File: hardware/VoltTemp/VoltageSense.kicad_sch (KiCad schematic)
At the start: 31 parts, among them J4 bms i2c test, SW1 BMS_BOOT, U1 EL3H7, U2 BQ7692003PW, U3 EL3H7, U4 ISO1641BDR

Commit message: schematic mostly done
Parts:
- removed C1: 4.7pF, Capacitor_SMD:C_0805_2012Metric, symbol Device:C_Small
- removed C3, C5: 1μF, Capacitor_SMD:C_0805_2012Metric, symbol Device:C_Small
- removed C4: 4.7μF, Capacitor_SMD:C_0805_2012Metric, symbol Device:C_Small
- removed R1, R6: 10kΩ, Resistor_SMD:R_0805_2012Metric, symbol Device:R
- removed R3, R4: 100Ω, Resistor_SMD:R_0805_2012Metric, symbol Device:R
- removed R7: 1kΩ, Resistor_SMD:R_0805_2012Metric, symbol Device:R
- removed U1, U3: EL3H7, Package_SO:SSOP-4_4.4x2.6mm_P1.27mm, symbol Isolator:SFH617A-1
- removed U2: BQ7692003PW, footprints:PW0020A_N, symbol BQ76920:BQ7692003PW
- removed U4: ISO1641BDR, footprints:SOIC8_D_TEX, symbol ISO1541QDQ1:ISO1641BDR
- added C18: 4.7uF, Capacitor_SMD:C_0805_2012Metric_Pad1.18x1.45mm_HandSolder, symbol Device:C
- added C24, C42: 0.1uF, Capacitor_SMD:C_0603_1608Metric_Pad1.08x0.95mm_HandSolder, symbol Device:C
- added C4: 4.7pF, Capacitor_SMD:C_0603_1608Metric_Pad1.08x0.95mm_HandSolder, symbol Device:C
- added C40, C41: 1uF, Capacitor_SMD:C_0603_1608Metric_Pad1.08x0.95mm_HandSolder, symbol Device:C
- added IC1: ISO1641BDR, VoltTemp:ISO1641BDR, symbol voltTemp:ISO1641BDR
- added R11, R13: 10kΩ, Resistor_SMD:R_0603_1608Metric_Pad0.98x0.95mm_HandSolder, symbol Device:R
- added R12: 1kΩ, Resistor_SMD:R_0603_1608Metric_Pad0.98x0.95mm_HandSolder, symbol Device:R
- added R59, R60: 100Ω, Resistor_SMD:R_0603_1608Metric_Pad0.98x0.95mm_HandSolder, symbol Device:R
- added U1, U3: EL3H7, UTSVT_ICs:EL3H7, symbol utsvt_ics:EL3H7
- added U2: BQ7692003PW, VoltTemp:BQ7692003PW, symbol voltTemp:BQ7692003PW
- R10, R9: footprint Resistor_SMD:R_0805_2012Metric -> Resistor_SMD:R_0603_1608Metric_Pad0.98x0.95mm_HandSolder; P/N CRCW080510K0FKEAC -> CRCW060310K0FKEI
- R2: value 500kΩ -> 510kΩ; footprint Resistor_SMD:R_0805_2012Metric -> Resistor_SMD:R_0603_1608Metric_Pad0.98x0.95mm_HandSolder; P/N 708-RNCF0805BTE500K -> CPF0603B510KE1
- R25, R26, R27, R28: footprint Resistor_SMD:R_0805_2012Metric -> Resistor_SMD:R_0603_1608Metric_Pad0.98x0.95mm_HandSolder; P/N SMD_0805 -> (none)
- R8: footprint Resistor_SMD:R_0805_2012Metric -> Resistor_SMD:R_0603_1608Metric_Pad0.98x0.95mm_HandSolder; P/N CRCW08051K00FKEAC -> CRCW06031K00FKEI
- SW1: value BMS_BOOT -> BOOT; footprint Button_Switch_SMD:SW_SPST_B3SL-1002P -> VoltTemp:SW_TL3365AF180QG; P/N 653-B3SL-1002P -> TL3365AF180QG
- TP1, TP2, TP3, TP4, TP5: footprint (none) -> TestPoint:TestPoint_Pad_1.0x1.0mm
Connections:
- net +3.3V: now also C24.1, IC1.1 (VCC1), U1.4
- net ALERT: now also R59.2, U2.20 (ALERT)
- net BAT: now also R60.2, U2.10 (BAT)
- net GND: now also C24.2, IC1.4 (GND1), R13.1
- net GND2: now also C18.2, C4.2, C40.2, C41.2, C42.2, IC1.5 (GND2), R11.1, U1.2, U2.18 (SRP), U2.19 (SRN), U2.3 (VSS)
- net I2C_SCL: now also IC1.3 (SCL1)
- net I2C_SDA: now also IC1.2 (SDA1)
- net LV_RTN: now also U3.2
- net VC0: now also U2.17 (VC0)
- net VC1: now also U2.16 (VC1)
- net VC2: now also U2.15 (VC2)
- net VC3: now also U2.14 (VC3)
- net VC4: now also U2.13 (VC4)
- net VC5: now also U2.12 (VC5)
- net bmSCL: now also IC1.6 (SCL2), U2.5 (SCL)
- net bmSDA: now also IC1.7 (SDA2), U2.4 (SDA)
- net bmsAlert: now also R13.2, U1.3
- net bmsBoot: now also SW1.1, R11.2, U2.6 (TS1), U3.4; no longer SW1.2
- net last_cell: now also R12.2
- net regout: now also SW1.2, C18.1, C42.1, IC1.8 (VCC2), U2.8 (REGOUT), U3.3; no longer SW1.1
- net at R5.2: now also U3.1
- net at R8.1: now also C40.1, U2.9 (REGSRC)
- net at D1.1 (K), R8.2: now also R12.1, R60.1
- new net: C4.1, R59.1, U1.1
- new net: C41.1, U2.7 (CAP1)
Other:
- moved on the sheet: J4, R8, R9

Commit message: most layout done
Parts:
- removed J4: bms i2c test, Connector_PinHeader_2.54mm:PinHeader_1x03_P2.54mm_Vertical, symbol Connector:Conn_01x03_Pin
- added R30: 0Ω, Resistor_SMD:R_0603_1608Metric_Pad0.98x0.95mm_HandSolder, symbol Device:R
- TP4: footprint TestPoint:TestPoint_Pad_1.0x1.0mm -> TestPoint:TestPoint_Keystone_5005-5009_Compact
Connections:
- net VC2: now also R30.2
- net VC3: now also R30.1
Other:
- moved on the sheet: R27, R28

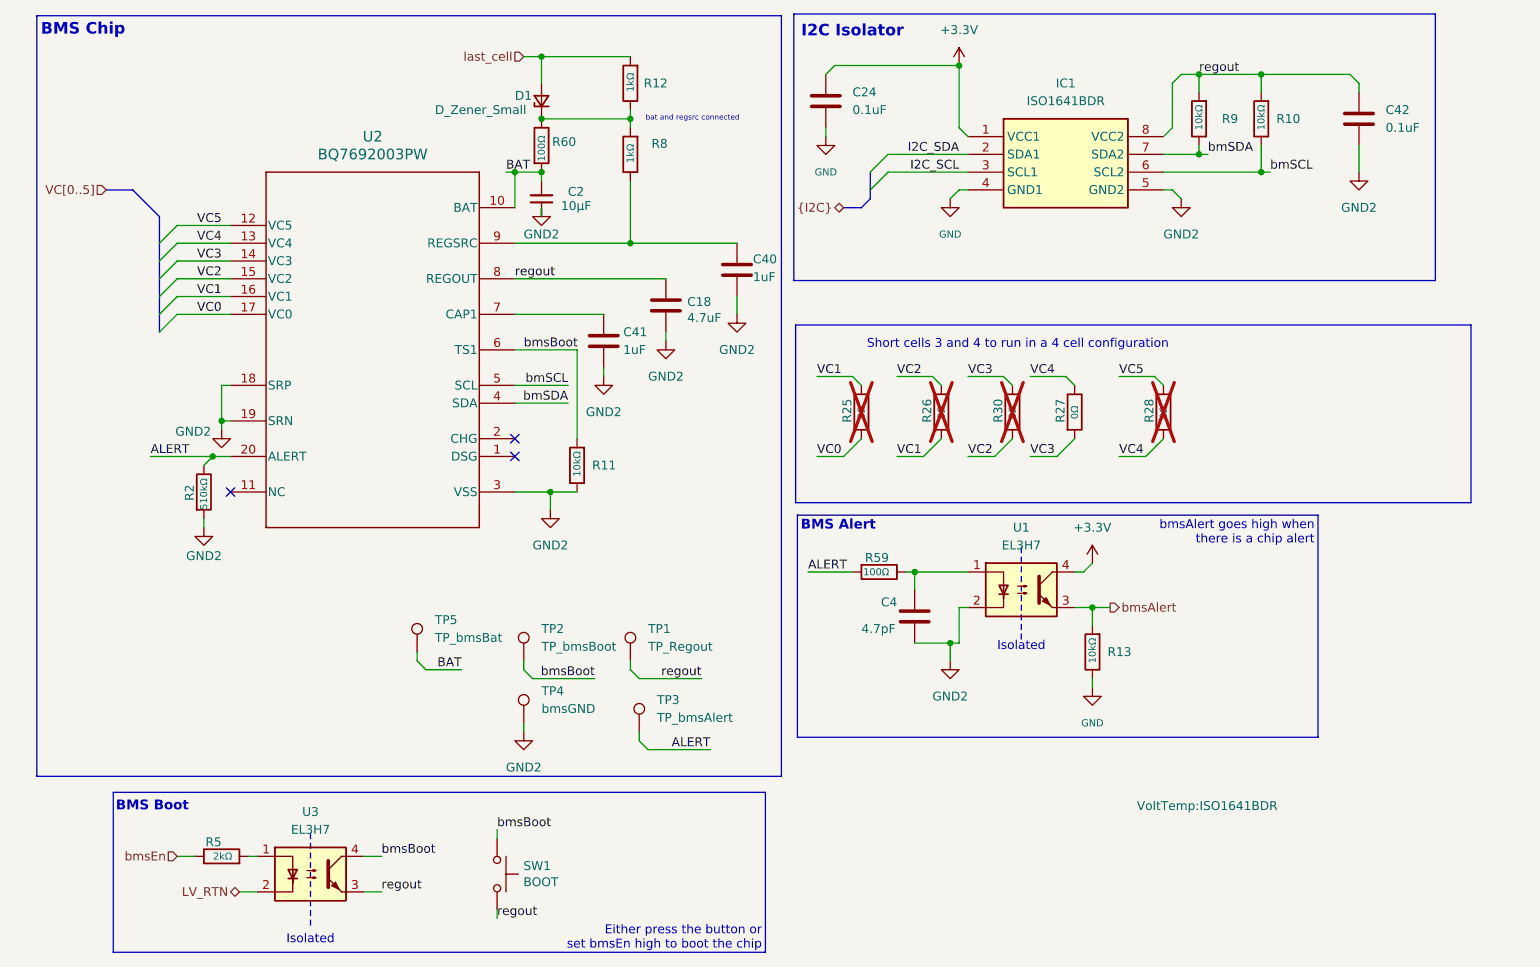
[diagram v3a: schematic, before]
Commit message: add thermistor test board, just need to route volttemp testpoints
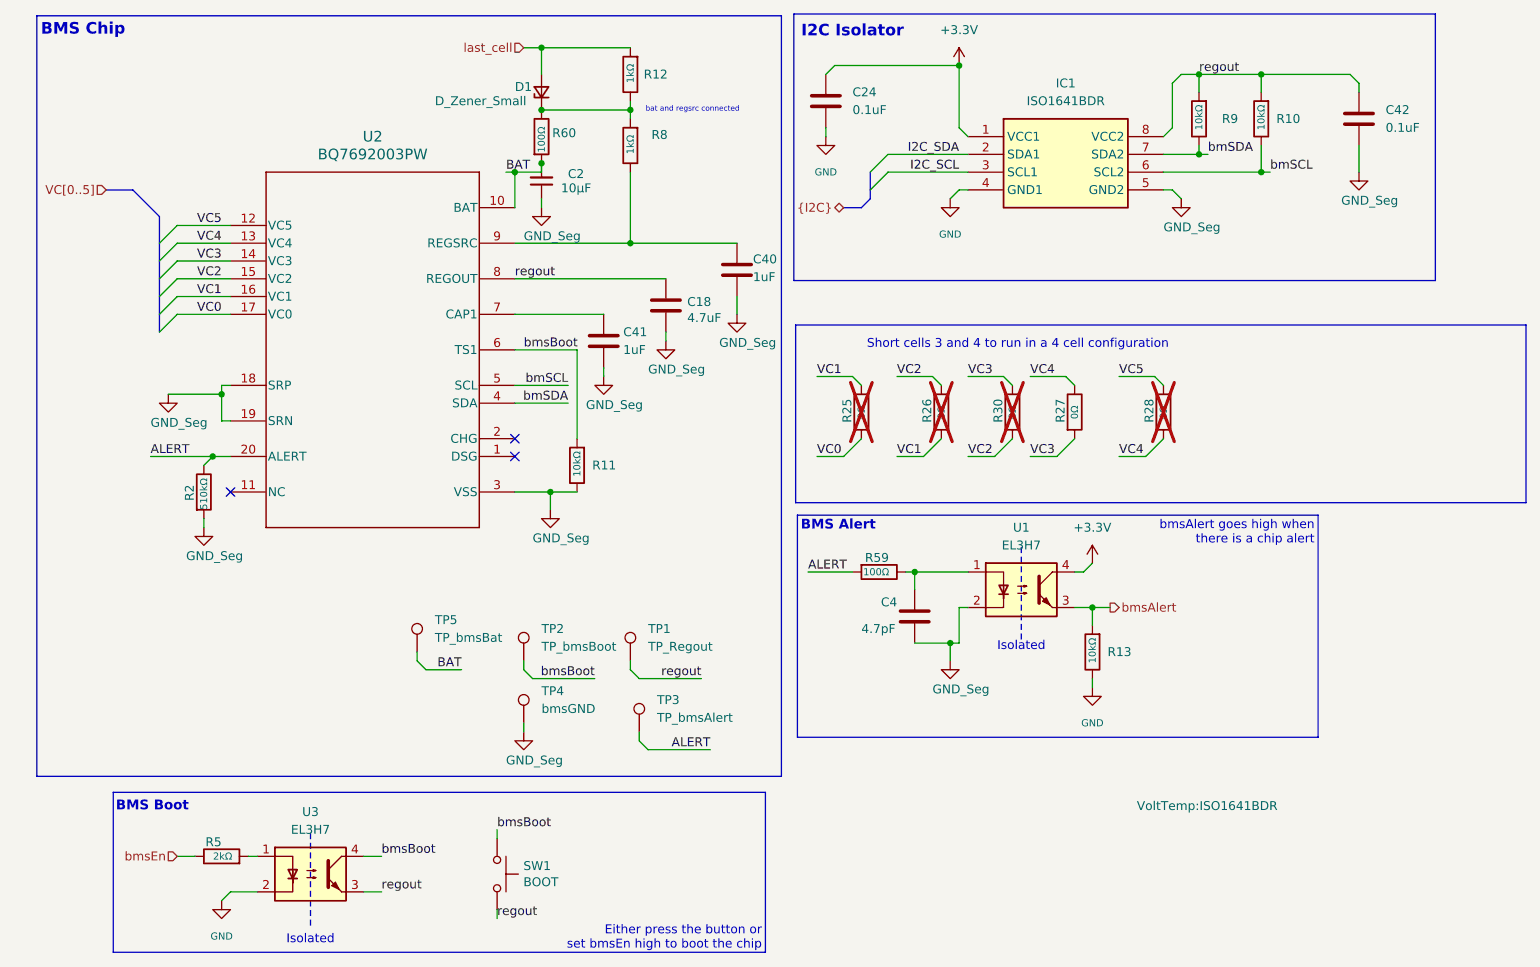
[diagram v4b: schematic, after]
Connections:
- net LV_RTN is gone; now on net GND: U3.2
- net GND2 renamed GND_Seg
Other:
- moved on the sheet: C2, D1, R12, R60, R8

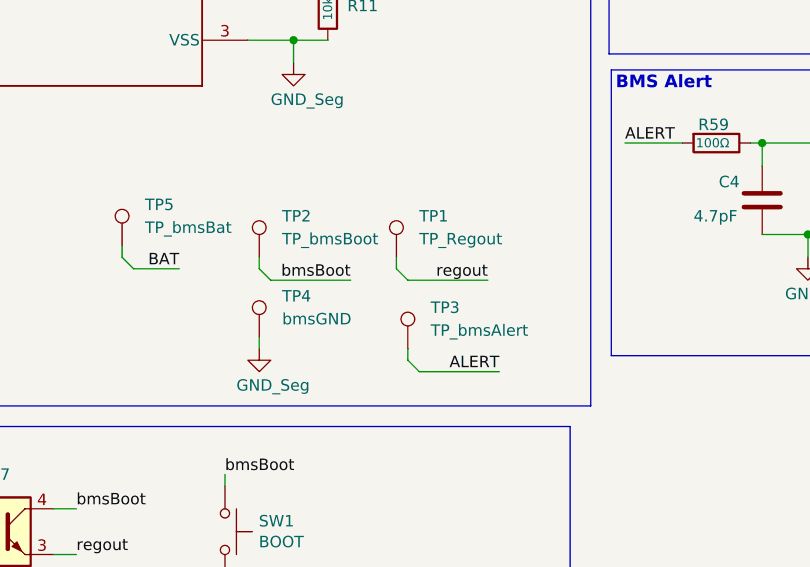
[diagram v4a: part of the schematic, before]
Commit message: voltage testpoints
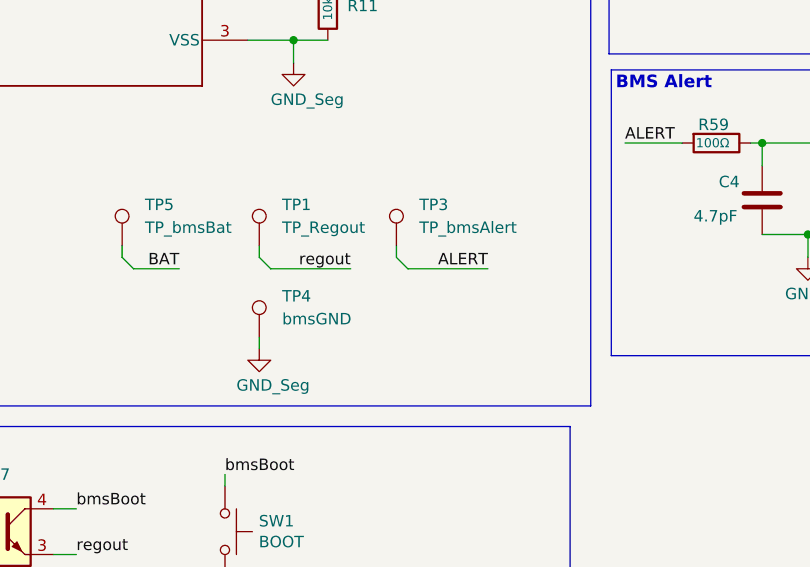
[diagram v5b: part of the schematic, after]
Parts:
- removed TP2: TP_bmsBoot, TestPoint:TestPoint_Pad_1.0x1.0mm, symbol Connector:TestPoint
- TP4: footprint TestPoint:TestPoint_Keystone_5005-5009_Compact -> TestPoint:TestPoint_Pad_1.0x1.0mm
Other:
- moved on the sheet: TP1, TP3

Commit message: done except for nanofit footprints
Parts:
- removed TP5: TP_bmsBat, TestPoint:TestPoint_Pad_1.0x1.0mm, symbol Connector:TestPoint
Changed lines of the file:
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@@
 	(wire
 		(pts
-			(xy 99.06 120.65) (xy 93.98 120.65)
-		)
-		(stroke
-			(width 0)
-			(type default)
-		)
-	)
-	(wire
-		(pts
 			(xy 170.18 111.76) (xy 170.18 116.84)
 		)
@@
 	(wire
 		(pts
-			(xy 93.98 120.65) (xy 92.71 119.38)
-		)
-		(stroke
-			(width 0)
-			(type default)
-		)
-	)
-	(wire
-		(pts
 			(xy 171.45 44.45) (xy 170.18 43.18)
 		)
@@
 	(wire
 		(pts
-			(xy 92.71 118.11) (xy 92.71 119.38)
-		)
-		(stroke
-			(width 0)
-			(type default)
-		)
-	)
-	(wire
-		(pts
 			(xy 58.42 69.85) (xy 66.04 69.85)
 		)
@@
 			"AQAAAAAAAAAAAAAAt0BwBwAAAAAkJQ0FAAAAAAAQAAAAAAAAsEwBSQEAAABQTAFJAQAAAAAAAAAA"
 			"AAAAoqlwBwAAAABl6QwFAAAAAAAQAAAAAAAA4EwBSQEAAACATAFJAQAAAAAAAAAAAAAASZdxBwAA"
-			"AAD2hgwFAAAAAAEQAAAAAAAAEE0BSQEAAACwTAFJAQAAAAQAAA=="
+			"AAD2hgwFAAAAAAEQAAAAAAAAEE0BSQEAAACwTAFJAQAAAAQAACABAAAAfHSx/lVZOY2g+LQgAQAA"
+			"AKD4tCABAAAARlZTxRTSi+3w+LQgAQAAAPD4tCABAAAARo2CgUmitlBA+bQgAQAAAED5tCABAAAA"
+			"c5fKxJZ20VlQqrUgAQAAAFCqtSABAAAAAjcfeojEjgawqrUgAQAAALCqtSABAAAAp50UXMvLStHw"
+			"5LQgAQAAAPDktCABAAAAwtcY6Y6FASmQ+bQgAQAAAJD5tCABAAAAsYca1okP8uHg+bQgAQAAAOD5"
+			"tCABAAAAfptUdGqYcSYw+rQgAQAAADD6tCABAAAA4qyh3Mv2NdkQq7UgAQAAABCrtSABAAAAH8Vi"
+			"Csg408GA+rQgAQAAAID6tCABAAAAwMkzM9y5YUpwq7UgAQAAAHCrtSABAAAAYdre9fH+lcnQ+rQg"
+			"AQAAAND6tCABAAAAA+ga3kaL5zsw57QgAQAAADDntCABAAAAQh3BtuobxKwg+7QgAQAAACD7tCAB"
+			"AAAAcnDTano9KGbw57QgAQAAAPDntCABAAAA6c0BeZtoOEVw+7QgAQAAAHD7tCABAAAADNjNSNTB"
+			"HazQq7UgAQAAANCrtSABAAAADnneNzTYKE7w6LQgAQAAAPDotCABAAAAYudeatMq9kLA+7QgAQAA"
+			"AMD7tCABAAAAbXbIuc1CTtsQ/LQgAQAAABD8tCABAAAAzV1QoSey4jJg/LQgAQAAAGD8tCABAAAA"
+			"KUZPGiZMP9uw/LQgAQAAALD8tCABAAAALS4FxldUe44A/bQgAQAAAAD9tCABAAAA0wXFLSjxCgRQ"
+			"/bQgAQAAAFD9tCABAAAAjOAq2487y/rw6rQgAQAAAPDqtCABAAAAm8irTzsmgc6g/bQgAQAAAKD9"
+			"tCABAAAA/gjH9h7KSCaw67QgAQAAALDrtCABAAAAQ5DOUOjVY5zw/bQgAQAAAPD9tCABAAAAq1iq"
+			"fnY36+xw7LQgAQAAAHDstCABAAAAPqNGhUFIl+9A/rQgAQAAAED+tCABAAAA/Up/n+Yze66Q/rQg"
+			"AQAAAJD+tCABAAAA80VyoGM/vrxw7bQgAQAAAHDttCABAAAAzzTYu+9VnLHg/rQgAQAAAOD+tCAB"
+			"AAAAq9mrnjjOtQUw/7QgAQAAADD/tCABAAAAfnQCzOBWpL6A/7QgAQAAAID/tCABAAAA1Le90h9J"
+			"Z3Uw0LQgAQAAADDQtCABAAAAJ9jmzoDm2jDw7rQgAQAAAPDutCABAAAAYsKPHGBdZFeA0LQgAQAA"
+			"AIDQtCABAAAA8WwpiPj7zLLQ0LQgAQAAANDQtCABAAAAUFAxtTIMonUg0bQgAQAAACDRtCABAAAA"
+			"xtU4KcvLYzRw0bQgAQAAAHDRtCABAAAAlO73pEXt6dyw4LUgAQ=="
 		)
 	)
@@
 			"AAAADA8AAAAAAADLk1cLAAAAALTmCgUAAAAADQ8AAAAAAAAnTVgLAAAAAJMLCwUAAAAADQ8AAAAA"
 			"AADBRVkLAAAAAIxyCwUAAAAAAAAAAAAAAADLRVkLAAAAAI9yCwUAAAAAAAAAAAAAAADdoVsLAAAA"
-			"ALfqCw=="
+			"ALfqC2tFWTA1WGxrNjQ2RFJ5a1REM1U0N1lpdTdKdFhQb2g4WGhkRHFrNDVZZDZwSk9ZNjZMSEdE"
+			"Z2YzNXlreVU4eFBOSDh3QUcxaXNHOVpiM2M0bkRKZlhEVUV4VWFRT1lRL3ZNbCt2dHhoS1BlVHFU"
+			"SlFWT1dNRmgzYTEzaXZ4SU1UY1dBdmxXK3laMHRMaS9DUjF4QTJoM3lrL0hrRDNRdjRpbVV5R2dQ"
+			"enRzZXJpTzh2eXZPb2pUaS9xamJ4R3EvM2RVWlpoRVdRV05WQmFXVnIvM2lpakVhM1RROWgzdEZK"
+			"YVdWS1hyeXZJY0FMNXh2bnpnWjNFRFpiM0JVYjhVZWhYNFJNODB0ZkFINmNzcjlBTmYzRUUzemV3"
+			"cE1kYUptNEloRUlwOVdUWGFMOVAyRHl3bkdnK2xTRjExb2I0ODdobG0xVFVod3VZM0thSTZINnRE"
+			"SnhneEEyMjZueHVLNk45NktzUE9XREJRYXA1UytLaU93aFAya1hjWVBkSlBaWnJhcEVBLzFYdmpJ"
+			"aWUvb1cvdy96UlZmV0xJeFQrVGJINWhZbU1aVmV4SW5CMFNpUDRpdXc2Z3M0azk4eUN1ajBtWWZ1"
+			"RjV6YWM5UkY0ZEdZZFJyY3JoelNpQ0RtQ1E3MVM3ODJ3YzJkVWsxSTZsN2doakJISEo5YlJSMHpR"
+			"NklOcFVLdi9hanl5YTlzdnRqWHdlamEzbThnRGhWb3R0a20yVEhiRURhRlBlT1JFenpsblJJUnVR"
+			"OU9wZ20vZ2o2L0xHdGszUGRJM3cwWlR1Vi85eUVkcytGWThwZ2s2U2o3MG0zOFdueTFPelNxOHVi"
+			"d2NYeFVKTUpKRFV1Zm9pZ052TE50YmRTVUx2LytIWVpzVDFpOFZDcGxHL21VeVY0K0ZsaDNHNFd4"
+			"cmxQSmVZdmxQTjRaNm9lUGMyS0ozU210YlRYemlCck1ldjkrQ2xsbEZDLy9rdnFnMVlDMmUybGdB"
+			"OGZINk1qVEpsVnJmZmpLM0xCaSsrYTJ1bWJUZjBzb0xwalkralgxSUlDTzN3dkx6bG1XU0Q5ZitS"
+			"cnNpaHVqcmdsT3pZSXUvTEc2eGFqeVg2ZnFNQjBxMm1ZVnJGblc3RUp4YjN0ZFlWbWEycXA2TDcx"
+			"bVVyZTIxTDVpQUN2R1doVEszOU1pYk42MVc3NVloUzVWSmRwQnVURk9NejNrRU52UTFqdklVV0hv"
+			"b3p1cWplNXFuSFJQeEJCdkdOMEVHa2I2c2FUczVTdmZZYktabm03YXpzNGtiVXN1ZDVnakU1NHFK"
+			"anFXMmJUcHZMRTg1eEEybTgwanUwM0FWNGdZYnV3Ui9wcFBzb3RMYU82VzNXVWMrWFlncVBvYkZh"
+			"SDZGdg=="
 		)
 	)
@@
 			"3KzSPWUklUH0OmbB3KzSvWUklUH0OmbB3KzSvWpDlUFBIWbB3KzSvWpDlUFBIWbB3KzSPWUklUH0"
 			"OmbB3KzSPXYDlUEOSGbB3KzSPXYDlUEOSGbB3KzSvXYDlUEOSGbB3KzSvWUklUH0OmbB3KzSvWUk"
-			"lUH0OmbB3KzSPXYDlUEOSGbB3KzSPazylEG0SWbB3KzSPazylEG0SWbB3KzSvQ=="
+			"lUH0OmbB3KzSPXYDlUEOSGbB3KzSPazylEG0SWbB3KzSPazylEG0SWbB3KzSvQAAAAAAAAAAAAAA"
+			"AAAAAAAAAAAAAAAAAAAAAAAAAAAAAAAAAAAAAAAAAAAAAAAAAAAAAAAAAAAAAAAAAAAAAAAAAAAA"
+			"AAAAAAAAAAAAAAAAAAAAAAAAAAAAAAAAAAAAAAAAAAAAAAAAAAAAAAAAAAAAAAAAAAAAAAAAAAAA"
+			"AAAAAAAAAAAAAAAAAAAAAAAAAAAAAAAAAAAAAAAAAAAAAAAAAAAAAAAAAAAAAAAAAAAAAAAAAAAA"
+			"AAAAAAAAAAAAAAAAAAAAAAAAAAAAAAAAAAAAAAAAAAAAAAAAAAAAAAAAAAAAAAAAAAAAAAAAAAAA"
+			"AAAAAAAAAAAAAAAAAAAAAAAAAAAAAAAAAAAAAAAAAAAAAAAAAAAAAAAAAAAAAAAAAAAAAAAAAAAA"
+			"AAAAAAAAAAAAAAAAAAAAAAAAAAAAAAAAAAAAAAAAAAAAAAAAAAAAAAAAAAAAAAAAAAAAAAAAAAAA"
+			"AAAAAAAAAAAAAAAAAAAAAAAAAAAAAAAAAAAAAAAAAAAAAAAAAAAAAAAAAAAAAAAAAAAAAAAAAAAA"
+			"AAAAAAAAAAAAAAAAAAAAAAAAAAAAAAAAAAAAAAAAAAAAAAAAAAAAAAAAAAAAAAAAAAAAAAAAAAAA"
+			"AAAAAAAAAAAAAAAAAAAAAAAAAAAAAAAAAAAAAAAAAAAAAAAAAAAAAAAAAAAAAAAAAAAAAAAAAAAA"
+			"AAAAAAAAAAAAAAAAAAAAAAAAAAAAAAAAAAAAAAAAAAAAAAAAAAAAAAAAAAAAAAAAAAAAAAAAAAAA"
+			"AAAAAAAAAAAAAAAAAAAAAAAAAAAAAAAAAAAAAAAAAAAAAAAAAAAAAAAAAAAAAAAAAAAAAAAAAAAA"
+			"AAAAAAAAAAAAAAAAAAAAAAAAAAAAAAAAAAAAAAAAAAAAAAAAAAAAAAAAAAAAAAAAAAAAAAAAAAAA"
+			"AAAAAAAAAAAAAAAAAAAAAAAAAAAAAAAAAAAAAAAAAAAAAAAAAAAAAAAAAAAAAAAAAAAAAAAAAAAA"
+			"AAAAAAAAAAAAAAAAAAAAAAAAAAAAAAAAAAAAAAAAAAAAAAAAAAAAAAAAAAAAAAAAAAAAAAAAAAAA"
+			"AAAAAAAAAAAAAAAAAAAAAAAAAAAAAAAAAAAAAAAAAAAAAAAAAAAAAAAAAAAAAAAAAAAAAAAAAAAA"
+			"AAAAAAAAAAAAAAAAAAAAAAAAAAAAAAAAAAAAAAAAAAAAAAAAAAAAAAAAAAAAAAAAAAAAAAAAAAAA"
+			"AAAAAAAAAAAAAAAAAAAAAAAAAAAAAAAAAAAAAAAAAAAAAAAAAAAAAAAAAAAAAAAAAAAAAAAAAAAA"
+			"AAAAAAAAAAAAAAAAAAAAAAAAAAAAAAAAAAAAAAAAAAAAAAAAAAAAAAAAAAAAAA=="
 		)
 	)
@@
 			"APERAAAAAAAAAIYETgEAAACghQROAQAAAAgAAAD/////xM7BCQAAAADEQY8FAAAAAPERAAAAAAAA"
 			"MIYETgEAAADQhQROAQAAAAQAAAD/////J9DBCQAAAACrW48FAAAAAPIRAAAAAAAAYIYETgEAAAAA"
-			"hgROAQAAAAAAAAD/////eOy/CQAAAACQdY8FAAAAAPIRAAAAAAAAkIYETgEAAAAwhgROAQAAAA=="
+			"hgROAQAAAAAAAAD/////eOy/CQAAAACQdY8FAAAAAPIRAAAAAAAAkIYETgEAAAAwhgROAQAAAAAA"
+			"AAAAAAAAAAAAAAAAAAAAAAAAAAAAAAAAAAAAAAAAAAAAAAAAAAAAAAAAAAAAAAAAAAAAAAAAAAAA"
+			"AAAAAAAAAAAAAAAAAAAAAAAAAAAAAAAAAAAAAAAAAAAAAAAAAAAAAAAAAAAAAAAAAAAAAAAAAAAA"
+			"AAAAAAAAAAAAAAAAAAAAAAAAAAAAAAAAAAAAAAAAAAAAAAAAAAAAAAAAAAAAAAAAAAAAAAAAAAAA"
+			"AAAAAAAAAAAAAAAAAAAAAAAAAAAAAAAAAAAAAAAAAAAAAAAAAAAAAAAAAAAAAAAAAAAAAAAAAAAA"
+			"AAAAAAAAAAAAAAAAAAAAAAAAAAAAAAAAAAAAAAAAAAAAAAAAAAAAAAAAAAAAAAAAAAAAAAAAAAAA"
+			"AAAAAAAAAAAAAAAAAAAAAAAAAAAAAAAAAAAAAAAAAAAAAAAAAAAAAAAAAAAAAAAAAAAAAAAAAAAA"
+			"AAAAAAAAAAAAAAAAAAAAAAAAAAAAAAAAAAAAAAAAAAAAAAAAAAAAAAAAAAAAAAAAAAAAAAAAAAAA"
+			"AAAAAAAAAAAAAAAAAAAAAAAAAAAAAAAAAAAAAAAAAAAAAAAAAAAAAAAAAAAAAAAAAAAAAAAAAAAA"
+			"AAAAAAAAAAAAAAAAAAAAAAAAAAAAAAAAAAAAAAAAAAAAAAAAAAAAAAAAAAAAAAAAAAAAAAAAAAAA"
+			"AAAAAAAAAAAAAAAAAAAAAAAAAAAAAAAAAAAAAAAAAAAAAAAAAAAAAAAAAAAAAAAAAAAAAAAAAAAA"
+			"AAAAAAAAAAAAAAAAAAAAAAAAAAAAAAAAAAAAAAAAAAAAAAAAAAAAAAAAAAAAAAAAAAAAAAAAAAAA"
+			"AAAAAAAAAAAAAAAAAAAAAAAAAAAAAAAAAAAAAAAAAAAAAAAAAAAAAAAAAAAAAAAAAAAAAAAAAAAA"
+			"AAAAAAAAAAAAAAAAAAAAAAAAAAAAAAAAAAAAAAAAAAAAAAAAAAAAAAAAAAAAAAAAAAAAAAAAAAAA"
+			"AAAAAAAAAAAAAAAAAAAAAAAAAAAAAAAAAAAAAAAAAAAAAAAAAAAAAAAAAAAAAAAAAAAAAAAAAAAA"
+			"AAAAAAAAAAAAAAAAAAAAAAAAAAAAAAAAAAAAAAAAAAAAAAAAAAAAAAAAAAAAAAAAAAAAAAAAAAAA"
+			"AAAAAAAAAAAAAAAAAAAAAAAAAAAAAAAAAAAAAAAAAAAAAAAAAAAAAAAAAAAAAAAAAAAAAAAAAAAA"
+			"AAAAAAAAAAAAAAAAAAAAAAAAAAAAAAAAAAAAAAAAAAAAAAAAAAAAAAAAAAAAAAAAAAAAAAAAAAAA"
+			"AAAAAAAAAAAAAAAAAAAAAAAAAAAAAAAAAAAAAAAAAAAAAAAAAAAAAAAAAAAAAAAAAAAAAAAAAA=="
 		)
 	)
@@
 		)
 	)
-	(label "BAT"
-		(at 99.06 120.65 180)
-		(effects
-			(font
-				(size 1.27 1.27)
-			)
-			(justify right bottom)
-		)
-	)
 	(label "VC1"
 		(at 64.77 67.31 180)
@@
 					(unit 1)
 				)
-			)
-		)
-	)
-	(symbol
-		(lib_id "Connector:TestPoint")
-		(at 92.71 118.11 0)
-		(unit 1)
-		(exclude_from_sim no)
-		(in_bom yes)
-		(on_board yes)
-		(dnp no)
-		(fields_autoplaced yes)
-		(property "Reference" "TP5"
-			(at 95.25 113.5379 0)
-			(effects
-				(font
-					(size 1.27 1.27)
-				)
-				(justify left)
-			)
-		)
-		(property "Value" "TP_bmsBat"
-			(at 95.25 116.0779 0)
-			(effects
-				(font
-					(size 1.27 1.27)
-				)
-				(justify left)
-			)
-		)
-		(property "Footprint" "TestPoint:TestPoint_Pad_1.0x1.0mm"
-			(at 97.79 118.11 0)
-			(effects
-				(font
-					(size 1.27 1.27)
-				)
-				(hide yes)
-			)
-		)
-		(property "Datasheet" "~"
-			(at 97.79 118.11 0)
-			(effects
-				(font
-					(size 1.27 1.27)
-				)
-				(hide yes)
-			)
-		)
-		(property "Description" "test point"
-			(at 92.71 118.11 0)
-			(effects
-				(font
-					(size 1.27 1.27)
-				)
-				(hide yes)
-			)
-		)
-		(pin "1"
-		)
-		(instances
-			(project "BPS-Voltage_Temp_Board"
-				(path "/286f0d93-2a80-4abf-b115-d33410b730c4/2e07b969-5a9c-4ef1-ba45-fc31f1004d05"
-					(reference "TP5")
-					(unit 1)
-				)
